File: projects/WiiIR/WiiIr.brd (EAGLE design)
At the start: 54.3 x 74.9 mm, 22 parts

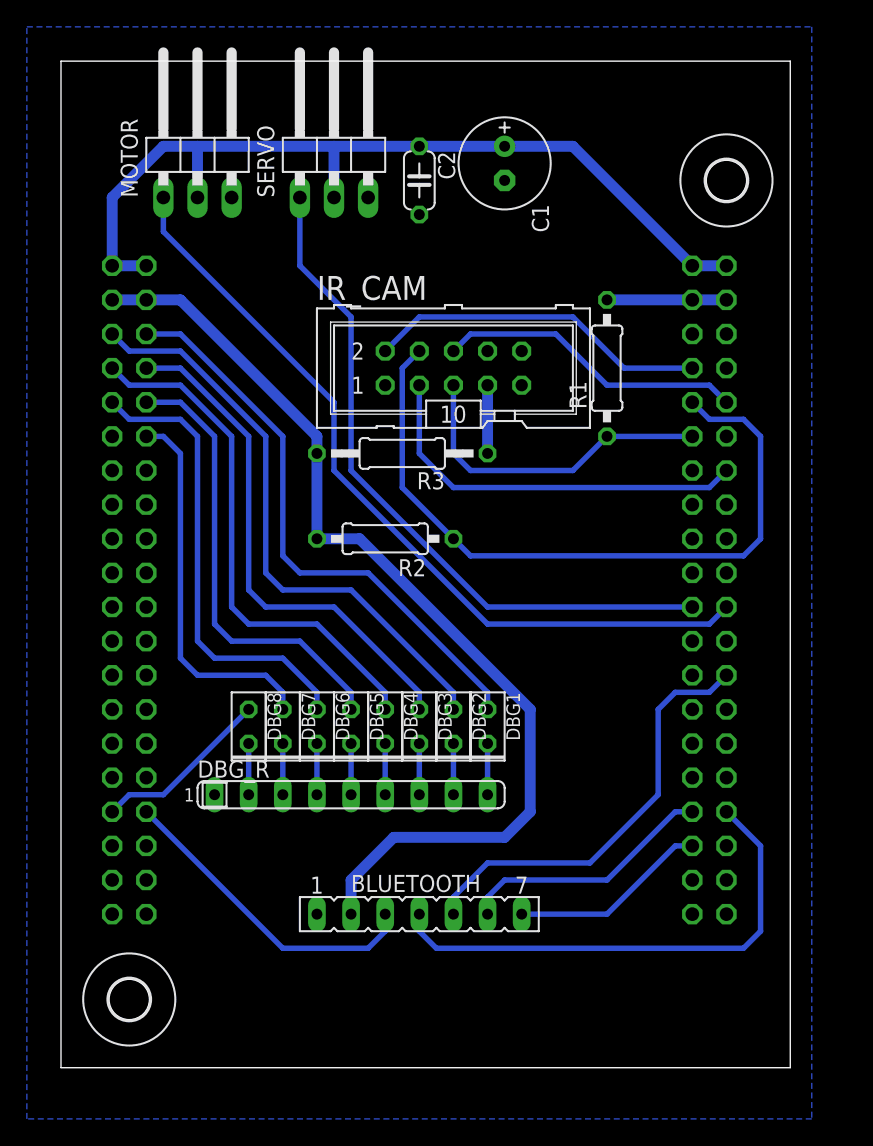
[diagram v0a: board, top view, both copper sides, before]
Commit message: Restructured + PCB v1 issues solved
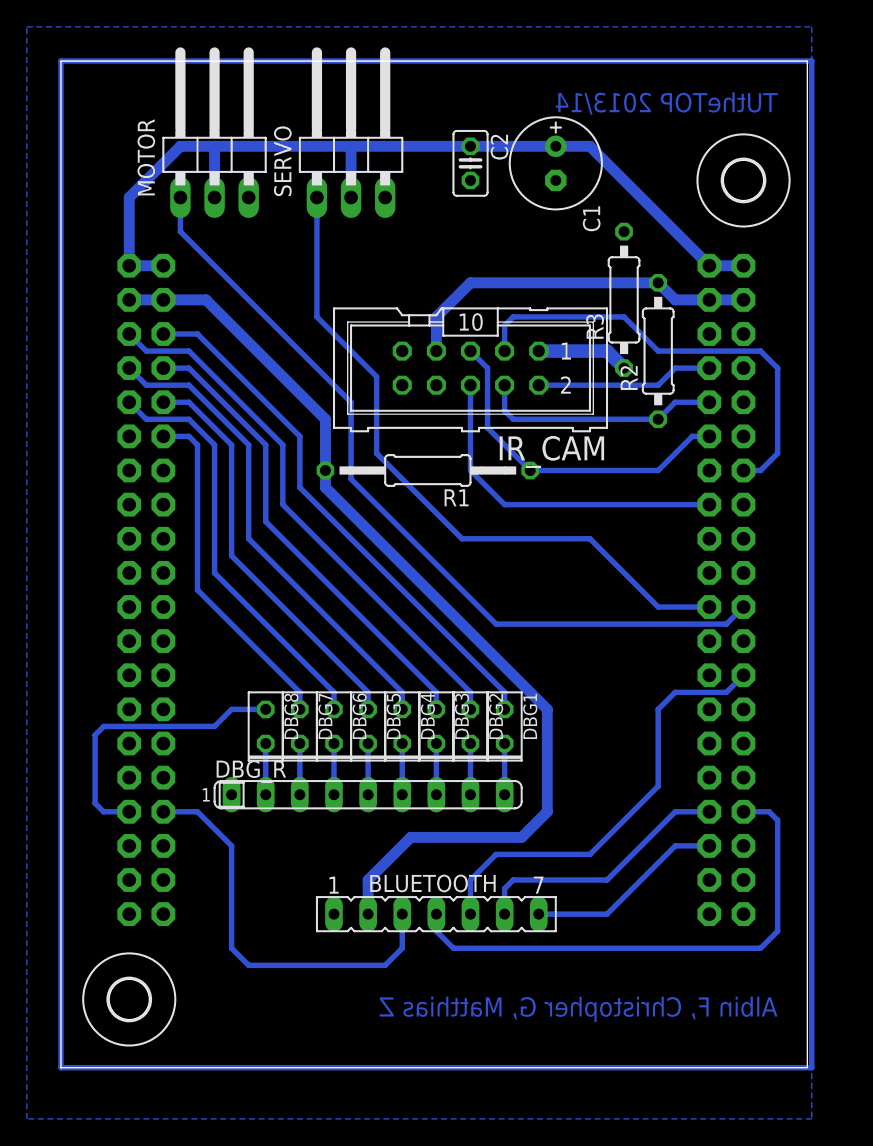
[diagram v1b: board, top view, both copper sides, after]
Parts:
- C2: device resistor:C050-024X044 -> resistor:C025-025X050
- R1: device resistor:0207/10 -> resistor:0207/15
- R3: device resistor:0207/12 -> resistor:0207/10
- SV1, SV2: device con-lstb:MA20-2 -> con-lstb:MA20-2BIG
- moved R2 24.7 mm to (44.5, 53.3), turned to 90 degrees
- moved R3 20.1 mm to (41.9, 57.1), turned to 90 degrees
- moved R1 15.4 mm to (27.3, 44.5), turned to 180 degrees
- moved C2 4.02 mm to (30.5, 67.3)
- moved C1 3.81 mm to (36.8, 67.3)
- moved DBG1 1.27 mm to (33.0, 25.4)
- moved SV2 1.27 mm to (49.5, 35.6)
- moved BLUETOOTH 1.27 mm to (27.9, 11.4)
- moved DBG2 1.27 mm to (30.5, 25.4)
- moved DBG3 1.27 mm to (27.9, 25.4)
- moved DBG4 1.27 mm to (25.4, 25.4)
- moved DBG5 1.27 mm to (22.9, 25.4)
- moved DBG6 1.27 mm to (20.3, 25.4)
- moved DBG7 1.27 mm to (17.8, 25.4)
- moved DBG8 1.27 mm to (15.2, 25.4)
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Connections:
- removed net N$1: IR_CAM.7, R3.1
- new net N$12: IR_CAM.1, R3.1
- net +3V3: now also IR_CAM.7; no longer R3.2
- net GND: now also R3.2; no longer IR_CAM.1
- net P0.2: no longer IR_CAM.6
- net P0.7: now also IR_CAM.6
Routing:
- net N$1: track 5.08 -> 261.6 mm
- net P0.5: track 53.7 -> 17.9 mm
- net P0.7: track 0.00 -> 25.2 mm
- net P0.2: track 23.0 -> 0.00 mm
- net +3V3: track 82.7 -> 99.3 mm
- net P0.3: track 25.5 -> 13.2 mm
- net P2.1: track 13.3 -> 21.4 mm
- net N$12: track 0.00 -> 6.88 mm
- net P2.10: track 23.8 -> 30.0 mm
- net P0.12: track 29.5 -> 33.5 mm
- net P3.2: track 33.6 -> 30.3 mm
- net P0.9: track 39.0 -> 35.7 mm
- net P3.1: track 34.4 -> 31.0 mm
- net P0.10: track 43.7 -> 40.3 mm
- net P0.1: track 38.3 -> 34.9 mm
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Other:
- board size 54.3 x 74.9 mm -> 55.5 x 74.9 mm

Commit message: IR_CAM description, optimizations
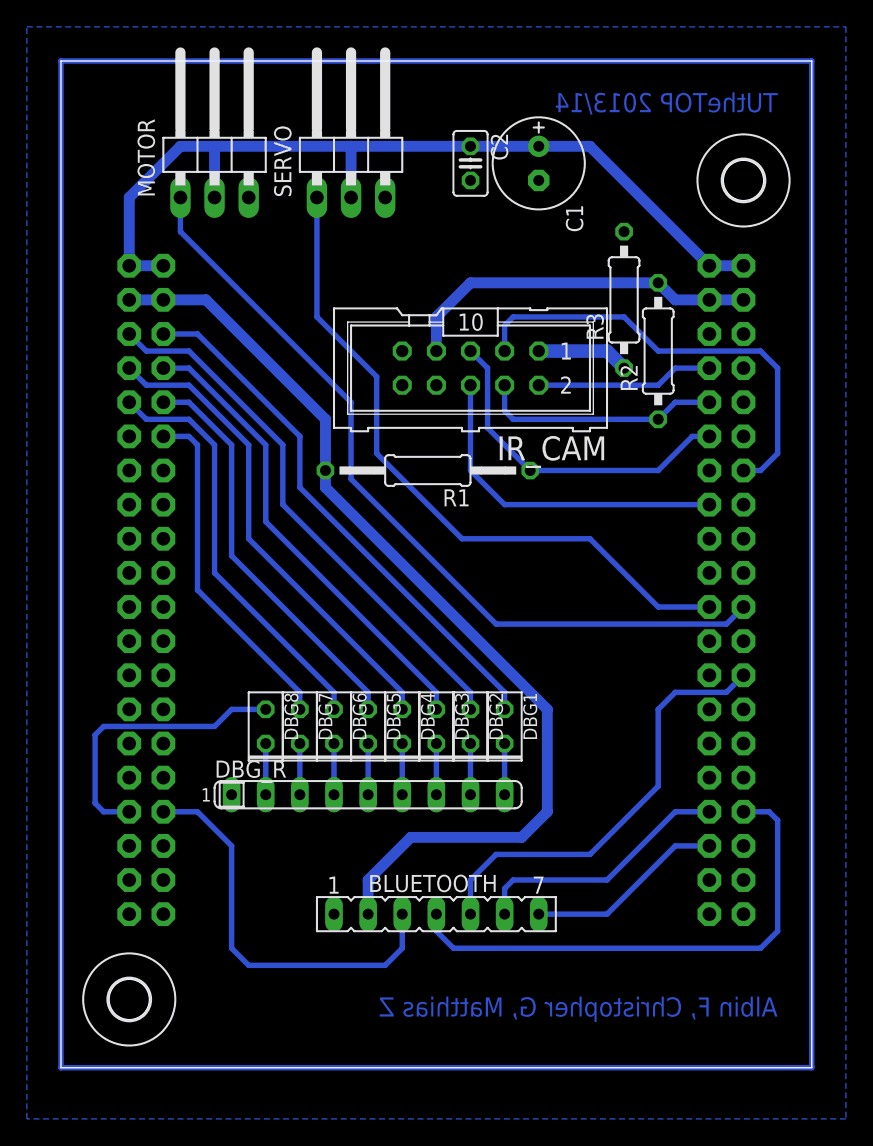
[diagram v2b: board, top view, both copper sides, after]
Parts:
- moved C1 1.27 mm to (35.6, 67.3)
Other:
- board size 55.5 x 74.9 mm -> 55.9 x 74.9 mm
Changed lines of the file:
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@@
 <board>
 <plain>
-<wire x1="0" y1="0" x2="55.55" y2="0" width="0" layer="20"/>
-<wire x1="55.55" y1="0" x2="55.55" y2="74.92" width="0" layer="20"/>
-<wire x1="55.55" y1="74.92" x2="0" y2="74.92" width="0" layer="20"/>
-<wire x1="0" y1="74.92" x2="0" y2="0" width="0" layer="20"/>
+<wire x1="0" y1="0" x2="55.88" y2="0" width="0" layer="20"/>
+<wire x1="55.88" y1="0" x2="55.88" y2="74.93" width="0" layer="20"/>
+<wire x1="55.88" y1="74.93" x2="0" y2="74.93" width="0" layer="20"/>
+<wire x1="0" y1="74.93" x2="0" y2="0" width="0" layer="20"/>
 <text x="53.34" y="71.12" size="1.4224" layer="16" font="vector" ratio="20" rot="MR0">TUtheTOP 2013/14</text>
 <text x="53.34" y="3.81" size="1.4224" layer="16" font="vector" ratio="20" rot="MR0">Albin F, Christopher G, Matthias Z</text>
@@
 </class>
 </classes>
-<designrules name="default">
+<designrules name="default *">
 <description language="de">&lt;b&gt;EAGLE Design Rules&lt;/b&gt;
 &lt;p&gt;
@@
 <param name="mtIsolate" value="1.5mm 0.15mm 0.2mm 0.15mm 0.2mm 0.15mm 0.2mm 0.15mm 0.2mm 0.15mm 0.2mm 0.15mm 0.2mm 0.15mm 0.2mm"/>
 <param name="mdWireWire" value="8mil"/>
-<param name="mdWirePad" value="8mil"/>
+<param name="mdWirePad" value="7mil"/>
 <param name="mdWireVia" value="8mil"/>
 <param name="mdPadPad" value="8mil"/>
@@
 <element name="U$1" library="holes" package="3,0" value="" x="5.08" y="5.08"/>
 <element name="U$2" library="holes" package="3,0" value="" x="50.8" y="66.04"/>
-<element name="C1" library="resistor" package="E2,5-7" value="100u" x="36.83" y="67.31" rot="R270"/>
+<element name="C1" library="resistor" package="E2,5-7" value="100u" x="35.56" y="67.31" rot="R270"/>
 <element name="C2" library="resistor" package="C025-025X050" value="100n" x="30.48" y="67.31" rot="R270"/>
 <element name="MOTOR" library="pinhead" package="1X03/90" value="" x="11.43" y="68.58"/>
@@
 <wire x1="11.43" y1="68.58" x2="21.59" y2="68.58" width="0.8128" layer="16"/>
 <wire x1="21.59" y1="68.58" x2="30.48" y2="68.58" width="0.8128" layer="16"/>
-<wire x1="30.48" y1="68.58" x2="36.83" y2="68.58" width="0.8128" layer="16"/>
-<wire x1="36.83" y1="68.58" x2="39.37" y2="68.58" width="0.8128" layer="16"/>
+<wire x1="30.48" y1="68.58" x2="35.56" y2="68.58" width="0.8128" layer="16"/>
+<wire x1="35.56" y1="68.58" x2="39.37" y2="68.58" width="0.8128" layer="16"/>
 <contactref element="MOTOR" pad="2"/>
 <contactref element="SERVO" pad="2"/>
@@
 <polygon width="0.4064" layer="16" isolate="0.254">
 <vertex x="-2.54" y="77.47"/>
-<vertex x="55.88" y="77.47"/>
-<vertex x="55.88" y="-3.81"/>
+<vertex x="58.42" y="77.47"/>
+<vertex x="58.42" y="-3.81"/>
 <vertex x="-2.54" y="-3.81"/>
 </polygon>

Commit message: Updated CamAdapter + Board
* Added 25 MHz resonator to adapter board
* Removed 25 MHz CLK signal from PCB connector
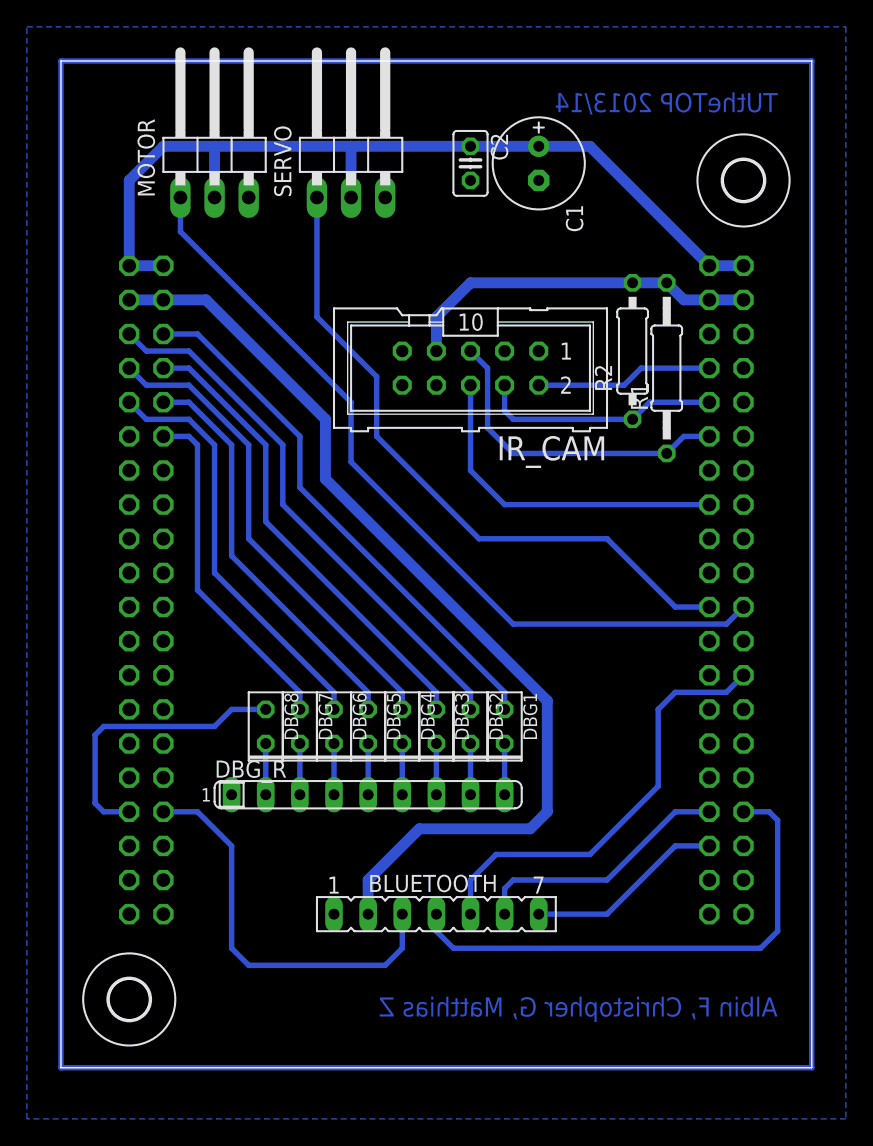
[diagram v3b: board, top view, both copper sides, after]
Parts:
- removed R3: 0, resistor:0207/10
- R1: device resistor:0207/15 -> resistor:0207/12
- SV1, SV2: device con-lstb:MA20-2BIG -> con-lstb:MA20-2
- moved R1 19.3 mm to (45.1, 52.1), turned to 90 degrees
- moved R2 1.91 mm to (42.5, 53.3)
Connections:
- removed net N$12: IR_CAM.1, R3.1
- net GND: now also IR_CAM.1; no longer R3.2
- net P0.12: no longer IR_CAM.3
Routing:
- net P0.12: track 33.5 -> 0.00 mm
- net N$12: track 6.88 -> 0.00 mm
- net P0.11: track 25.1 -> 24.1 mm
- net P1.1: track 60.4 -> 59.7 mm
- net +5V: track 66.2 -> 67.0 mm
- net P1.2: track 50.4 -> 49.6 mm

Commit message: Rev 2.0 RC
* TODO: Check CamAdapter.brd quarz oscillator package
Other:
- board text added: "rev 2.0"
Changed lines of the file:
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@@
 <text x="53.34" y="71.12" size="1.4224" layer="16" font="vector" ratio="20" rot="MR0">TUtheTOP 2013/14</text>
 <text x="53.34" y="3.81" size="1.4224" layer="16" font="vector" ratio="20" rot="MR0">Albin F, Christopher G, Matthias Z</text>
+<text x="10.16" y="71.12" size="1.4224" layer="16" font="vector" ratio="20" rot="MR0">rev 2.0</text>
 </plain>
 <attributes>

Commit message: Final
* finally found out pcb2gcode and CAM settings so that
  lower right corner is origin and coordinates relative to that point
	lign up when CNC milling
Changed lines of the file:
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@@
 <board>
 <plain>
-<wire x1="0" y1="0" x2="55.88" y2="0" width="0" layer="20"/>
-<wire x1="55.88" y1="0" x2="55.88" y2="74.93" width="0" layer="20"/>
-<wire x1="55.88" y1="74.93" x2="0" y2="74.93" width="0" layer="20"/>
-<wire x1="0" y1="74.93" x2="0" y2="0" width="0" layer="20"/>
+<wire x1="0" y1="0" x2="55.88" y2="0" width="0.0508" layer="20"/>
+<wire x1="55.88" y1="0" x2="55.88" y2="74.93" width="0.0508" layer="20"/>
+<wire x1="55.88" y1="74.93" x2="0" y2="74.93" width="0.0508" layer="20"/>
+<wire x1="0" y1="74.93" x2="0" y2="0" width="0.0508" layer="20"/>
 <text x="53.34" y="71.12" size="1.4224" layer="16" font="vector" ratio="20" rot="MR0">TUtheTOP 2013/14</text>
 <text x="53.34" y="3.81" size="1.4224" layer="16" font="vector" ratio="20" rot="MR0">Albin F, Christopher G, Matthias Z</text>
